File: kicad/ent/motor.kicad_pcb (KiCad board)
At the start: 2 copper layers, 99.9 x 78.7 mm, 28 parts, among them J10 Conn_01x02_Male, J11 Conn_01x02_Male, J12 Barrel_Jack, J13 Conn_01x12_Male, J14 Conn_01x12_Male, J8 Conn_01x02_Male, J9 Conn_01x02_Male, U4 IFX9201SGAUMA1, U5 IFX9201SGAUMA1, U6 IFX9201SGAUMA1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

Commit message: pcb's
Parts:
- moved J13 35.5 mm to (88.4, 42.0)
- moved J14 23.0 mm to (122.4, 42.0)
- moved C10 22.7 mm to (86.2, 103.5)
- moved C11 22.7 mm to (107.1, 103.5)
- moved C14 22.7 mm to (72.0, 97.7)
- moved C12 22.7 mm to (127.9, 103.5)
- moved C13 22.7 mm to (148.5, 103.9)
- moved C15 22.7 mm to (75.2, 103.5)
- moved C16 22.7 mm to (96.0, 103.5)
- moved C17 22.7 mm to (116.8, 103.5)
- moved C20 22.7 mm to (92.8, 97.7)
- moved C22 22.7 mm to (113.8, 97.7)
- moved C24 22.7 mm to (134.5, 97.7)
- moved U4 22.7 mm to (80.6, 96.1)
- moved U5 22.7 mm to (101.5, 96.1)
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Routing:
- net VOS: track 0.00 -> 165.4 mm, vias 0 -> 9
- net SPI1_MOSI: track 0.00 -> 133.1 mm, vias 0 -> 5
- net SPI1_SCK: track 0.00 -> 133.0 mm, vias 0 -> 5
- net SPI1_MISO: track 0.00 -> 129.4 mm, vias 0 -> 4
- net Net-(J14-Pad5): track 0.00 -> 126.6 mm, vias 0 -> 4
- net NSS1: track 0.00 -> 94.9 mm, vias 0 -> 2
- net NSS4: track 0.00 -> 82.6 mm
- net DIR4: track 0.00 -> 81.8 mm, vias 0 -> 4
- net NSS2: track 0.00 -> 79.2 mm, vias 0 -> 2
- net PWM4: track 0.00 -> 75.4 mm, vias 0 -> 2
- net PWM3: track 0.00 -> 64.1 mm, vias 0 -> 2
- net NSS3: track 0.00 -> 63.3 mm, vias 0 -> 1
- net DIR1: track 0.00 -> 62.4 mm, vias 0 -> 1
- net PWM1: track 0.00 -> 62.0 mm, vias 0 -> 1
- net DIR3: track 0.00 -> 61.6 mm, vias 0 -> 2
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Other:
- outline, holes or cut-outs redrawn
- board text added: "PWM"
- board text added: "SPI"

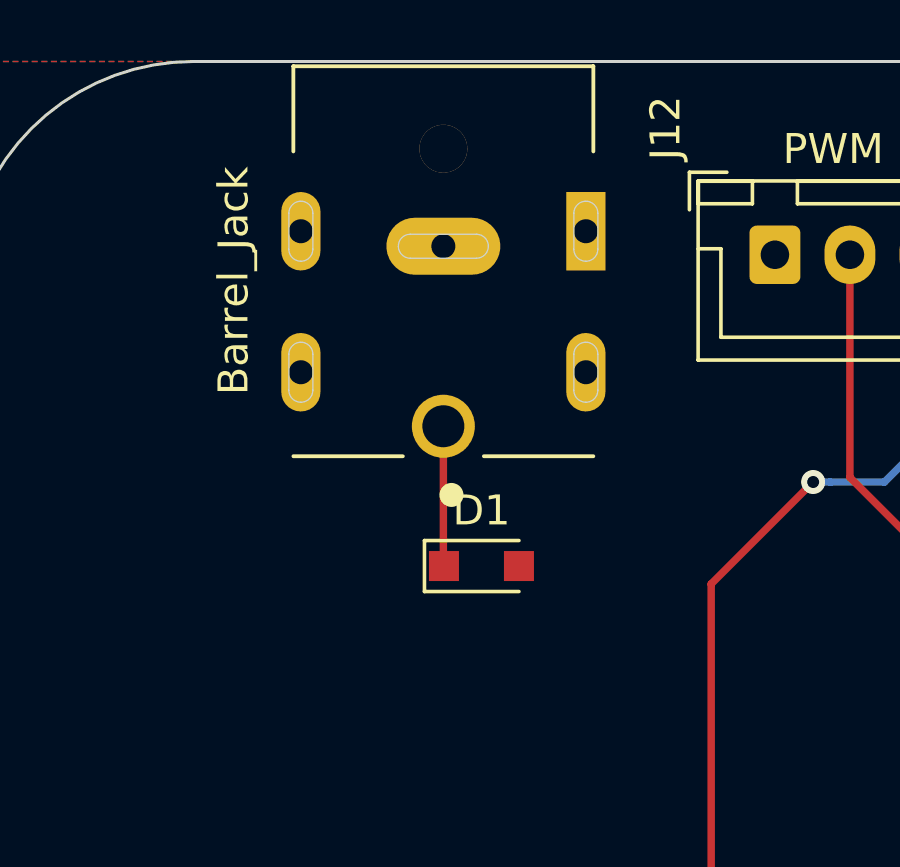
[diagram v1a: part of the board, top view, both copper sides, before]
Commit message: barreljack footprint update
naar de footprint van mouser veranderd
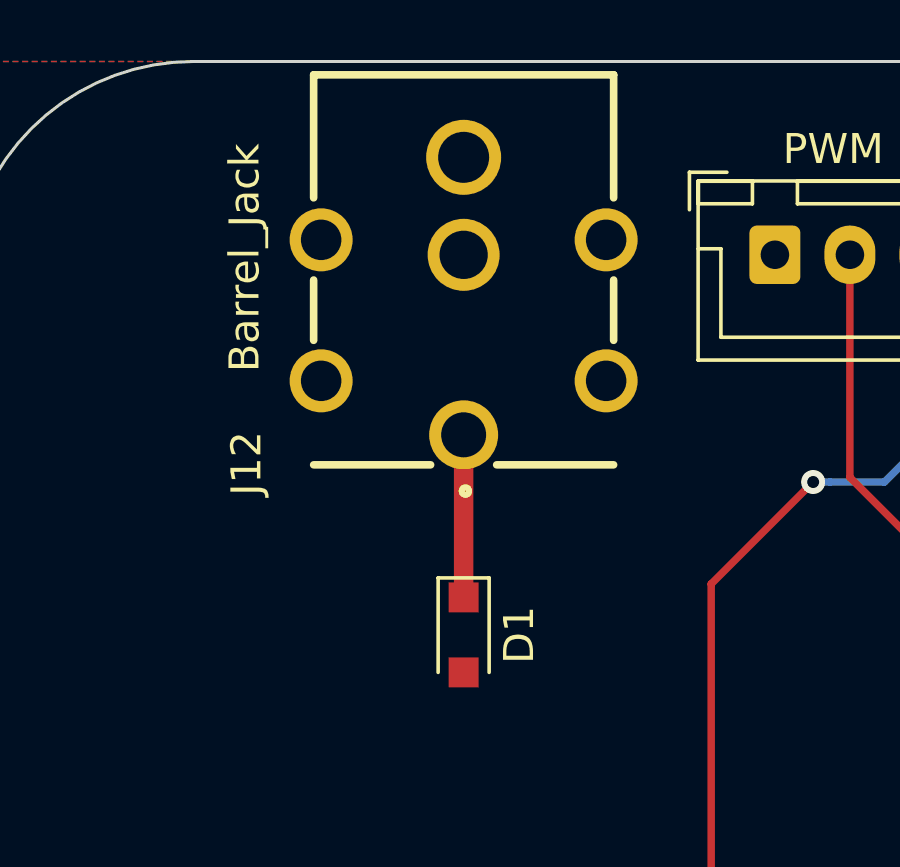
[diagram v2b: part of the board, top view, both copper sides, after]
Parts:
- J12: footprint PJ-082BH:CUI_PJ-082BH -> SamacSys_Parts:PJ-082BH
- moved J12 6.25 mm to (78.0, 36.0)
- moved D1 2.37 mm to (78.0, 54.7), turned to 270 degrees
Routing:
- net +12V: track 94.0 -> 94.7 mm

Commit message: pcb done
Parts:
- added H5: MountingHole_Pad, MountingHole:MountingHole_2.2mm_M2_Pad, F.Cu at (67.7, 41.9)
- added H6: MountingHole_Pad, MountingHole:MountingHole_2.2mm_M2_Pad, F.Cu at (67.7, 108.0)
- added H7: MountingHole_Pad, MountingHole:MountingHole_2.2mm_M2_Pad, F.Cu at (156.6, 42.2)
- added H8: MountingHole_Pad, MountingHole:MountingHole_2.2mm_M2_Pad, F.Cu at (156.6, 108.0)
- moved C21 29.8 mm to (110.4, 109.2)
- moved C23 29.8 mm to (130.9, 109.0)
- moved C19 29.8 mm to (89.8, 109.2)
- moved C9 11.2 mm to (68.7, 85.3)
- moved C22 2.16 mm to (113.7, 95.5), turned to 90 degrees
- moved C20 2.16 mm to (92.8, 95.5), turned to 90 degrees
- moved C24 2.16 mm to (134.5, 95.5), turned to 90 degrees
- turned C10 to 270 degrees
- turned C11 to 270 degrees
- turned C12 to 270 degrees
- turned C13 to 270 degrees
- turned C15 to 270 degrees
- turned C16 to 270 degrees
- turned C17 to 270 degrees
- turned C18 to 270 degrees
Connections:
- J12 pad 7: (no net) -> GND
- U4 pad 13: (no net) -> GND
- U5 pad 13: (no net) -> GND
- U6 pad 13: (no net) -> GND
- U7 pad 13: (no net) -> GND
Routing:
- net +12V: track 94.7 -> 20.6 mm
- net GND: track 2.53 -> 23.9 mm, vias 0 -> 100
- net M4OUT2: track 9.19 -> 12.6 mm
- net M1OUT2: track 8.90 -> 12.1 mm
- net M3OUT2: track 9.21 -> 12.3 mm
- net M2OUT2: track 9.01 -> 12.1 mm
- net M1OUT1: track 11.5 -> 12.9 mm
- net M2OUT1: track 11.6 -> 12.9 mm
- net M3OUT1: track 11.9 -> 13.1 mm
- net M4OUT1: track 12.5 -> 13.7 mm
- net SPI1_MISO: track 129.4 -> 130.5 mm
- added copper zone on F.Cu, net +12V
- added copper zone on B.Cu, net GND
- removed copper zone on B.Cu, net +12V

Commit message: gerbers
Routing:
- net VOS: vias 9 -> 10
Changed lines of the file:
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@@
     (thickness 1.6)
     (drawings 15)
-    (tracks 461)
+    (tracks 463)
     (zones 0)
     (modules 32)
@@
   )
   (setup
-    (last_trace_width 0.65)
+    (last_trace_width 0.25)
     (user_trace_width 0.65)
     (trace_clearance 0.2)
@@
     (pcbplotparams
       (layerselection 0x010fc_ffffffff)
-      (usegerberextensions false)
+      (usegerberextensions true)
       (usegerberattributes false)
       (usegerberadvancedattributes false)
@@
       (outputformat 1)
       (mirror false)
-      (drillshape 1)
+      (drillshape 0)
       (scaleselection 1)
       (outputdirectory ""))
@@
   (segment (start 113.793 96.639) (end 113.792 96.638) (width 0.25) (layer F.Cu) (net 2))
   (via (at 136.429 94.652) (size 0.8) (drill 0.4) (layers F.Cu B.Cu) (net 3))
+  (segment (start 115.529 94.652) (end 116.094685 94.652) (width 0.25) (layer B.Cu) (net 3))
+  (segment (start 116.094685 94.652) (end 136.429 94.652) (width 0.25) (layer B.Cu) (net 3))
+  (segment (start 138.329 94.639) (end 136.442 94.639) (width 0.25) (layer F.Cu) (net 3))
+  (segment (start 136.442 94.639) (end 136.429 94.652) (width 0.25) (layer F.Cu) (net 3))
   (via (at 94.629 94.652) (size 0.8) (drill 0.4) (layers F.Cu B.Cu) (net 3))
+  (segment (start 94.629 94.652) (end 96.66 94.652) (width 0.25) (layer F.Cu) (net 3))
+  (segment (start 96.66 94.652) (end 96.673 94.639) (width 0.25) (layer F.Cu) (net 3))
   (via (at 73.579 94.652) (size 0.8) (drill 0.4) (layers F.Cu B.Cu) (net 3))
+  (segment (start 73.579 94.652) (end 74.144685 94.652) (width 0.25) (layer B.Cu) (net 3))
+  (segment (start 74.144685 94.652) (end 94.629 94.652) (width 0.25) (layer B.Cu) (net 3))
+  (segment (start 75.845 94.639) (end 73.592 94.639) (width 0.25) (layer F.Cu) (net 3))
+  (segment (start 73.592 94.639) (end 73.579 94.652) (width 0.25) (layer F.Cu) (net 3))
   (via (at 115.529 94.652) (size 0.8) (drill 0.4) (layers F.Cu B.Cu) (net 3))
-  (segment (start 73.592 94.639) (end 73.579 94.652) (width 0.25) (layer F.Cu) (net 3))
-  (segment (start 75.845 94.639) (end 73.592 94.639) (width 0.25) (layer F.Cu) (net 3))
-  (segment (start 96.66 94.652) (end 96.673 94.639) (width 0.25) (layer F.Cu) (net 3))
-  (segment (start 94.629 94.652) (end 96.66 94.652) (width 0.25) (layer F.Cu) (net 3))
   (segment (start 117.488 94.652) (end 117.501 94.639) (width 0.25) (layer F.Cu) (net 3))
   (segment (start 115.529 94.652) (end 117.488 94.652) (width 0.25) (layer F.Cu) (net 3))
-  (segment (start 136.442 94.639) (end 136.429 94.652) (width 0.25) (layer F.Cu) (net 3))
-  (segment (start 138.329 94.639) (end 136.442 94.639) (width 0.25) (layer F.Cu) (net 3))
-  (segment (start 74.144685 94.652) (end 94.629 94.652) (width 0.25) (layer B.Cu) (net 3))
-  (segment (start 73.579 94.652) (end 74.144685 94.652) (width 0.25) (layer B.Cu) (net 3))
   (segment (start 94.629 94.652) (end 115.529 94.652) (width 0.25) (layer B.Cu) (net 3))
-  (segment (start 116.094685 94.652) (end 136.429 94.652) (width 0.25) (layer B.Cu) (net 3))
-  (segment (start 115.529 94.652) (end 116.094685 94.652) (width 0.25) (layer B.Cu) (net 3))
-  (segment (start 110.854 42.002) (end 110.854 51.077) (width 0.25) (layer B.Cu) (net 3))
   (via (at 110.854 51.077) (size 0.8) (drill 0.4) (layers F.Cu B.Cu) (net 3))
-  (segment (start 110.854 41.877) (end 114.054 38.677) (width 0.25) (layer B.Cu) (net 3))
-  (segment (start 110.854 42.002) (end 110.854 41.877) (width 0.25) (layer B.Cu) (net 3))
-  (segment (start 144.929 40.777) (end 144.929 42.002) (width 0.25) (layer B.Cu) (net 3))
-  (segment (start 142.829 38.677) (end 144.929 40.777) (width 0.25) (layer B.Cu) (net 3))
-  (segment (start 114.054 38.677) (end 142.829 38.677) (width 0.25) (layer B.Cu) (net 3))
   (segment (start 110.854 51.642685) (end 111.729 52.517685) (width 0.25) (layer F.Cu) (net 3))
   (segment (start 110.854 51.077) (end 110.854 51.642685) (width 0.25) (layer F.Cu) (net 3))
@@
   (segment (start 109.179 83.737) (end 109.179 81.477) (width 0.25) (layer B.Cu) (net 3))
   (segment (start 115.529 90.087) (end 109.179 83.737) (width 0.25) (layer B.Cu) (net 3))
+  (segment (start 110.854 42.002) (end 110.854 51.077) (width 0.25) (layer B.Cu) (net 3))
+  (segment (start 144.929 40.777) (end 143.522 39.37) (width 0.25) (layer B.Cu) (net 3))
+  (segment (start 144.929 42.002) (end 144.929 40.777) (width 0.25) (layer B.Cu) (net 3))
+  (via (at 133.731 39.37) (size 0.8) (drill 0.4) (layers F.Cu B.Cu) (net 3))
+  (segment (start 143.522 39.37) (end 133.731 39.37) (width 0.25) (layer B.Cu) (net 3))
+  (segment (start 110.854 40.777) (end 110.854 42.002) (width 0.25) (layer F.Cu) (net 3))
+  (segment (start 112.261 39.37) (end 110.854 40.777) (width 0.25) (layer F.Cu) (net 3))
+  (segment (start 133.731 39.37) (end 112.261 39.37) (width 0.25) (layer F.Cu) (net 3))
   (via (at 108.229 97.652) (size 0.8) (drill 0.4) (layers F.Cu B.Cu) (net 4))
   (via (at 128.929 97.652) (size 0.8) (drill 0.4) (layers F.Cu B.Cu) (net 4))
